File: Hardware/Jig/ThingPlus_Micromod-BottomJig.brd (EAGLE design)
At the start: 124.5 x 83.8 mm, 111 parts, among them J1 USB_A_PTH_MALE, J5 USB_A_SMT_FEMALE, J7 QWIIC_RIGHT_ANGLE, U1 TB_MAIN_BRAIN_CARDEDGE_TB_SIDE, U2 74LVC4066, U4 74LVC4066_MUX_1:1_X4

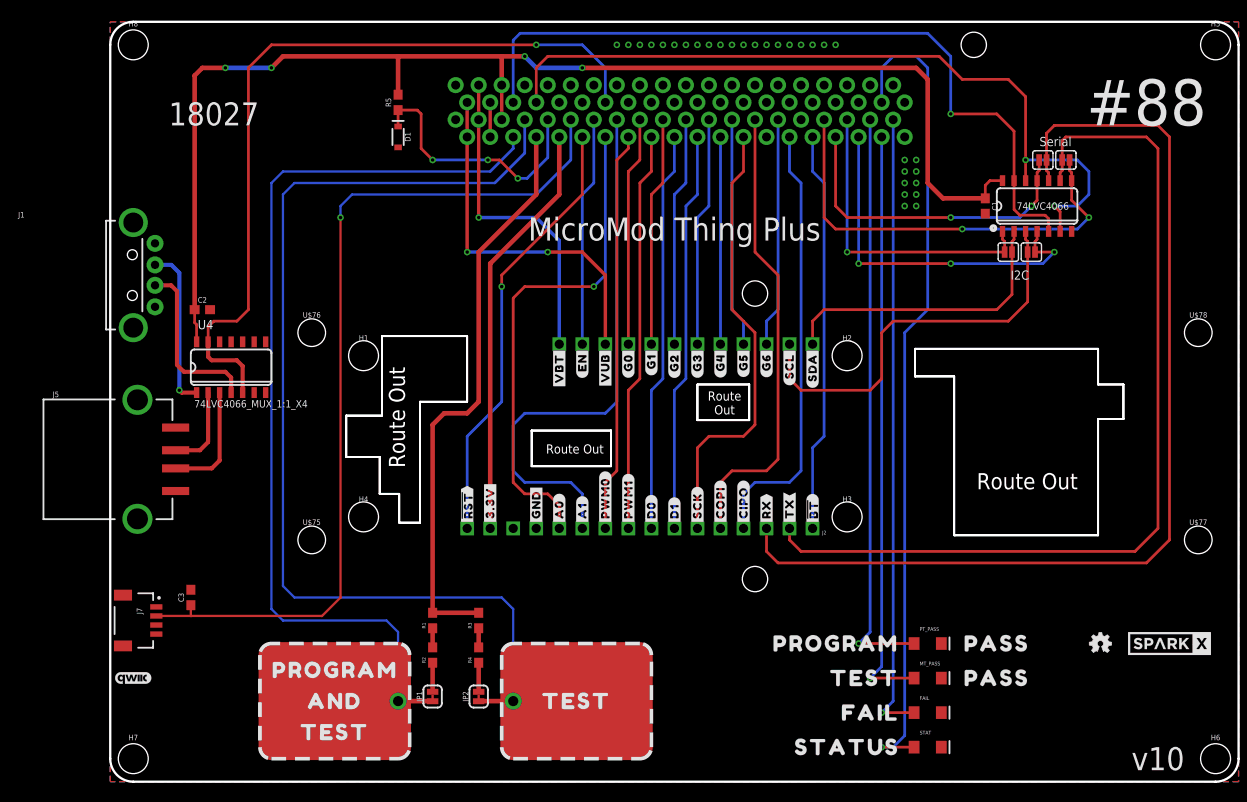
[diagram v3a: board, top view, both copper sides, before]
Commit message: Updated board and middle jig
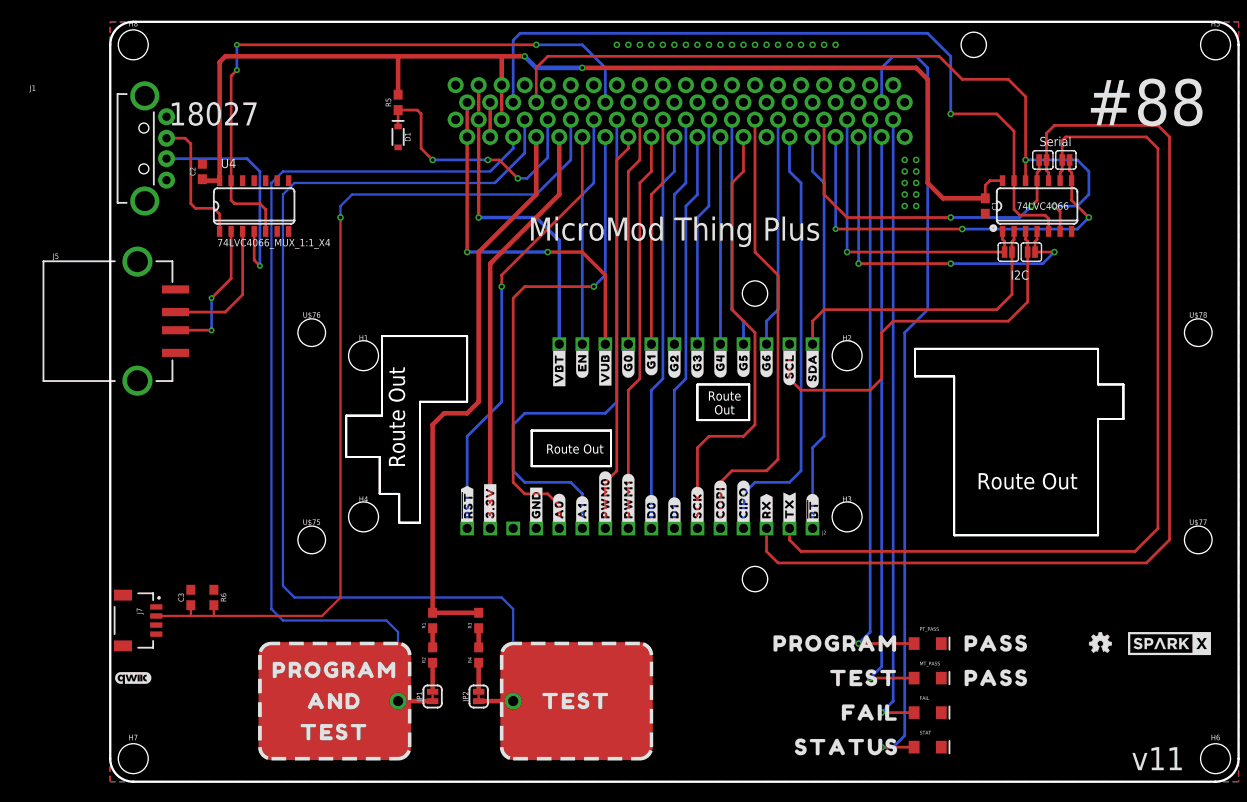
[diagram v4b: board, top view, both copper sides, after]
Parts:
- added R6: 10k, SparkFun-Resistors:0603
- moved U4 18.0 mm to (24.1, 69.8)
- moved J5 15.2 mm to (8.89, 57.1)
- moved C2 15.2 mm to (19.1, 73.7), turned to 90 degrees
- moved J1 14.0 mm to (12.7, 76.2)
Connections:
- net BRD_USB_D+: now also J5.D+; no longer J5.D-
- net BRD_USB_D-: now also J5.D-; no longer J5.D+
- net GND: now also R6.1
- net J_RX1-I: now also U1.P15; no longer U1.P13
- net J_TX1-O: now also U1.P13; no longer U1.P15
- net MICROMOD_QWIIC_PWR: now also R6.2
- net MICROMOD_RX: now also J2.3, J_SDA.2, U2.10; no longer J2.2, J_SCL1.2, U2.9
- net MICROMOD_TX: now also J2.2, J_SCL1.2, U2.9; no longer J2.3, J_SDA.2, U2.10
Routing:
- net USB_SWCH_EN: track 87.6 -> 69.6 mm, vias 1 -> 3
- net BRAIN_VCC: track 145.5 -> 127.7 mm, vias 4 -> 2
- net MICROMOD_TX: track 112.8 -> 101.2 mm
- net MICROMOD_RX: track 101.2 -> 112.8 mm
- net BRD_USB_D+: track 9.41 -> 15.8 mm, vias 0 -> 2
- net USB_D-: track 19.0 -> 25.4 mm, vias 0 -> 1
- net USB_D+: track 18.0 -> 15.1 mm, vias 1 -> 0
- net BRD_USB_D-: track 12.7 -> 15.2 mm
- net J_TX1-O: track 48.3 -> 45.9 mm, vias 2 -> 3
- net J_RX1-I: track 35.7 -> 38.1 mm
- net MICROMOD_QWIIC_PWR: track 97.5 -> 98.7 mm
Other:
- board text added: "v11"
- board text removed: "v10"
